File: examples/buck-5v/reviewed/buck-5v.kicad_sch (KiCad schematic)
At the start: 11 parts, among them J1 12V IN, J2 5V OUT, U1 LM2596S-5

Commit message: Route the sheets, and anchor the ground vias where the loop is
The user's verdict on the last round stood: none of the five schematics
read as a human drawing, and the artwork still had its physics wrong.
This round answers both.

The schematic side replaces the stub-and-label sheet with a router.
Every signal net becomes a tree of straight, L-, Z- and detour-shaped
runs on the 1.27 mm grid: legs leave a pin along its own stub, escape
distances stagger so a bus does not fight over one column, every pin
reserves a runway another wire may cross but not ride along, and the
sheet frame, title block and notes are obstacles like any symbol.
Fragments merge Kruskal-style so a rail whose regulator is boxed in
still gets its capacitors chained; each surviving fragment keeps one
label, because the label is what names the net. Collinear same-net
segments are unioned and then split at every tee - KiCad 9's
connectivity requires files drawn the way the editor draws them, with
a junction dot and a wire break wherever a branch tees in, and a wire
that runs through a junction connects on one side of it only. That
last fact cost an evening and is now a comment.

Trying to draw the wires found what no rule had: the buck's LED was
upside down with its ground pointing up into the resistor above it,
both breakout headers faced away from everything they connect to
(fixed with mirrored symbols, which Part now supports), the FPGA
sheet's notes printed over the 1.2 V regulator, and its programming
header sat inside the title block. Wired: buck, motor and op-amp
completely; the Pico carrier 31 of 33 nets; the FPGA board 16 of 19 -
what stays labelled is what a human would label too.

The artwork side anchors every FPGA decoupling capacitor's ground via
against its own pad, on the far side from the supply pad, with the
1.2 mm stub as the whole loop - retiring all seven
layout.decoupling_via findings and that waiver with them. A back_cost
experiment (0.4 to 0.6) to shrink the return-path cuts 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
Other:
- moved on the sheet: D2
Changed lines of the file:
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@@
   	(comment 2 "from tools/make_examples.py in sabas0ba/kicad_skills")
   )
+  (wire (pts (xy 199.39 77.47) (xy 199.39 82.55)) (stroke (width 0) (type default)))
+  (wire (pts (xy 124.46 68.58) (xy 124.46 76.2)) (stroke (width 0) (type default)))
+  (wire (pts (xy 124.46 76.2) (xy 134.62 76.2)) (stroke (width 0) (type default)))
+  (wire (pts (xy 134.62 59.69) (xy 134.62 76.2)) (stroke (width 0) (type default)))
+  (wire (pts (xy 134.62 59.69) (xy 154.94 59.69)) (stroke (width 0) (type default)))
+  (junction (at 134.62 76.2) (diameter 0) (color 0 0 0 0))
   (wire (pts (xy 33.02 66.04) (xy 30.48 66.04)) (stroke (width 0) (type default)))
   (symbol (lib_id "power:+12V") (at 30.48 66.04 90) (unit 1)
@@
   )
   (wire (pts (xy 137.16 76.2) (xy 134.62 76.2)) (stroke (width 0) (type default)))
-  (label "SW" (at 134.62 76.2 0) (effects (font (size 1.27 1.27)) (justify left bottom)))
   (wire (pts (xy 144.78 76.2) (xy 147.32 76.2)) (stroke (width 0) (type default)))
   (symbol (lib_id "power:GND") (at 147.32 76.2 270) (unit 1)
@@
   )
   (wire (pts (xy 154.94 62.23) (xy 154.94 59.69)) (stroke (width 0) (type default)))
-  (label "SW" (at 154.94 59.69 0) (effects (font (size 1.27 1.27)) (justify left bottom)))
   (wire (pts (xy 154.94 69.85) (xy 154.94 72.39)) (stroke (width 0) (type default)))
   (symbol (lib_id "power:+5V") (at 154.94 72.39 0) (unit 1)
@@
     (instances (project "buck-5v" (path "/ec98644d-848c-5056-a4cb-c829189be5c3" (reference "R1") (unit 1))))
   )
-  (wire (pts (xy 199.39 85.09) (xy 199.39 82.55)) (stroke (width 0) (type default)))
-  (symbol (lib_id "power:GND") (at 199.39 82.55 180) (unit 1)
-    (exclude_from_sim no) (in_bom no) (on_board yes) (dnp no)
-    (property "Reference" "#PWR18" (at 199.39 82.55 0) (effects (font (size 1.27 1.27)) hide))
-    (property "Value" "GND" (at 199.39 78.74 0) (effects (font (size 1.27 1.27))))
-    (property "Footprint" "" (at 199.39 82.55 0) (effects (font (size 1.27 1.27)) hide))
-    (property "Datasheet" "" (at 199.39 82.55 0) (effects (font (size 1.27 1.27)) hide))
+  (wire (pts (xy 199.39 92.71) (xy 199.39 95.25)) (stroke (width 0) (type default)))
+  (symbol (lib_id "power:GND") (at 199.39 95.25 0) (unit 1)
+    (exclude_from_sim no) (in_bom no) (on_board yes) (dnp no)
+    (property "Reference" "#PWR18" (at 199.39 95.25 0) (effects (font (size 1.27 1.27)) hide))
+    (property "Value" "GND" (at 199.39 99.06 0) (effects (font (size 1.27 1.27))))
+    (property "Footprint" "" (at 199.39 95.25 0) (effects (font (size 1.27 1.27)) hide))
+    (property "Datasheet" "" (at 199.39 95.25 0) (effects (font (size 1.27 1.27)) hide))
     (pin "1" (uuid "3235223e-d87f-580f-9e80-34d8bd5b48e9-p"))
     (instances (project "buck-5v" (path "/ec98644d-848c-5056-a4cb-c829189be5c3" (reference "#PWR18") (unit 1))))
   )
-  (wire (pts (xy 199.39 92.71) (xy 199.39 95.25)) (stroke (width 0) (type default)))
-  (label "LED_A" (at 199.39 95.25 0) (effects (font (size 1.27 1.27)) (justify left bottom)))
-  (symbol (lib_id "Device:LED") (at 199.39 88.9 270.0) (unit 1)
+  (wire (pts (xy 199.39 85.09) (xy 199.39 82.55)) (stroke (width 0) (type default)))
+  (symbol (lib_id "Device:LED") (at 199.39 88.9 90.0) (unit 1)
     (exclude_from_sim no) (in_bom yes) (on_board yes) (dnp no)
     (property "Reference" "D2" (at 199.39 82.55 0) (effects (font (size 1.27 1.27))))
@@
     (instances (project "buck-5v" (path "/ec98644d-848c-5056-a4cb-c829189be5c3" (reference "J2") (unit 1))))
   )
-  (wire (pts (xy 53.34 118.11) (xy 53.34 120.65)) (stroke (width 0) (type default)) (uuid "50121226-b759-5cf7-9474-3f9038b2192a-w"))
-  (label "+12V" (at 53.34 120.65 0) (effects (font (size 1.27 1.27)) (justify left bottom)) (uuid "50121226-b759-5cf7-9474-3f9038b2192a-l"))
-  (symbol (lib_id "power:PWR_FLAG") (at 53.34 118.11 0) (unit 1)
-    (exclude_from_sim no) (in_bom no) (on_board yes) (dnp no)
-    (property "Reference" "#FLG01" (at 53.34 118.11 0) (effects (font (size 1.27 1.27)) hide))
-    (property "Value" "PWR_FLAG" (at 53.34 114.3 0) (effects (font (size 1.27 1.27))))
-    (property "Footprint" "" (at 53.34 118.11 0) (effects (font (size 1.27 1.27)) hide))
-    (property "Datasheet" "" (at 53.34 118.11 0) (effects (font (size 1.27 1.27)) hide))
+  (wire (pts (xy 74.92999999999999 35.56) (xy 74.92999999999999 38.1)) (stroke (width 0) (type default)) (uuid "50121226-b759-5cf7-9474-3f9038b2192a-w"))
+  (label "+12V" (at 74.92999999999999 38.1 0) (effects (font (size 1.27 1.27)) (justify left bottom)) (uuid "50121226-b759-5cf7-9474-3f9038b2192a-l"))
+  (symbol (lib_id "power:PWR_FLAG") (at 74.92999999999999 35.56 0) (unit 1)
+    (exclude_from_sim no) (in_bom no) (on_board yes) (dnp no)
+    (property "Reference" "#FLG01" (at 74.92999999999999 35.56 0) (effects (font (size 1.27 1.27)) hide))
+    (property "Value" "PWR_FLAG" (at 74.92999999999999 31.750000000000004 0) (effects (font (size 1.27 1.27))))
+    (property "Footprint" "" (at 74.92999999999999 35.56 0) (effects (font (size 1.27 1.27)) hide))
+    (property "Datasheet" "" (at 74.92999999999999 35.56 0) (effects (font (size 1.27 1.27)) hide))
     (pin "1" (uuid "50121226-b759-5cf7-9474-3f9038b2192a-p"))
     (instances (project "buck-5v" (path "/ec98644d-848c-5056-a4cb-c829189be5c3" (reference "#FLG01") (unit 1))))
   )
-  (wire (pts (xy 68.58 118.11) (xy 68.58 120.65)) (stroke (width 0) (type default)) (uuid "826d4f09-5262-50fb-a7d7-fd8ef58ef78c-w"))
-  (label "GND" (at 68.58 120.65 0) (effects (font (size 1.27 1.27)) (justify left bottom)) (uuid "826d4f09-5262-50fb-a7d7-fd8ef58ef78c-l"))
-  (symbol (lib_id "power:PWR_FLAG") (at 68.58 118.11 0) (unit 1)
-    (exclude_from_sim no) (in_bom no) (on_board yes) (dnp no)
-    (property "Reference" "#FLG02" (at 68.58 118.11 0) (effects (font (size 1.27 1.27)) hide))
-    (property "Value" "PWR_FLAG" (at 68.58 114.3 0) (effects (font (size 1.27 1.27))))
-    (property "Footprint" "" (at 68.58 118.11 0) (effects (font (size 1.27 1.27)) hide))
-    (property "Datasheet" "" (at 68.58 118.11 0) (effects (font (size 1.27 1.27)) hide))
+  (wire (pts (xy 90.17 35.56) (xy 90.17 38.1)) (stroke (width 0) (type default)) (uuid "826d4f09-5262-50fb-a7d7-fd8ef58ef78c-w"))
+  (label "GND" (at 90.17 38.1 0) (effects (font (size 1.27 1.27)) (justify left bottom)) (uuid "826d4f09-5262-50fb-a7d7-fd8ef58ef78c-l"))
+  (symbol (lib_id "power:PWR_FLAG") (at 90.17 35.56 0) (unit 1)
+    (exclude_from_sim no) (in_bom no) (on_board yes) (dnp no)
+    (property "Reference" "#FLG02" (at 90.17 35.56 0) (effects (font (size 1.27 1.27)) hide))
+    (property "Value" "PWR_FLAG" (at 90.17 31.750000000000004 0) (effects (font (size 1.27 1.27))))
+    (property "Footprint" "" (at 90.17 35.56 0) (effects (font (size 1.27 1.27)) hide))
+    (property "Datasheet" "" (at 90.17 35.56 0) (effects (font (size 1.27 1.27)) hide))
     (pin "1" (uuid "826d4f09-5262-50fb-a7d7-fd8ef58ef78c-p"))
     (instances (project "buck-5v" (path "/ec98644d-848c-5056-a4cb-c829189be5c3" (reference "#FLG02") (unit 1))))
   )
-  (wire (pts (xy 83.82 118.11) (xy 83.82 120.65)) (stroke (width 0) (type default)) (uuid "838852d4-b251-5697-b727-47601c00fcad-w"))
-  (label "+5V" (at 83.82 120.65 0) (effects (font (size 1.27 1.27)) (justify left bottom)) (uuid "838852d4-b251-5697-b727-47601c00fcad-l"))
-  (symbol (lib_id "power:PWR_FLAG") (at 83.82 118.11 0) (unit 1)
-    (exclude_from_sim no) (in_bom no) (on_board yes) (dnp no)
-    (property "Reference" "#FLG03" (at 83.82 118.11 0) (effects (font (size 1.27 1.27)) hide))
-    (property "Value" "PWR_FLAG" (at 83.82 114.3 0) (effects (font (size 1.27 1.27))))
-    (property "Footprint" "" (at 83.82 118.11 0) (effects (font (size 1.27 1.27)) hide))
-    (property "Datasheet" "" (at 83.82 118.11 0) (effects (font (size 1.27 1.27)) hide))
+  (wire (pts (xy 105.41 35.56) (xy 105.41 38.1)) (stroke (width 0) (type default)) (uuid "838852d4-b251-5697-b727-47601c00fcad-w"))
+  (label "+5V" (at 105.41 38.1 0) (effects (font (size 1.27 1.27)) (justify left bottom)) (uuid "838852d4-b251-5697-b727-47601c00fcad-l"))
+  (symbol (lib_id "power:PWR_FLAG") (at 105.41 35.56 0) (unit 1)
+    (exclude_from_sim no) (in_bom no) (on_board yes) (dnp no)
+    (property "Reference" "#FLG03" (at 105.41 35.56 0) (effects (font (size 1.27 1.27)) hide))
+    (property "Value" "PWR_FLAG" (at 105.41 31.750000000000004 0) (effects (font (size 1.27 1.27))))
+    (property "Footprint" "" (at 105.41 35.56 0) (effects (font (size 1.27 1.27)) hide))
+    (property "Datasheet" "" (at 105.41 35.56 0) (effects (font (size 1.27 1.27)) hide))
     (pin "1" (uuid "838852d4-b251-5697-b727-47601c00fcad-p"))
     (instances (project "buck-5v" (path "/ec98644d-848c-5056-a4cb-c829189be5c3" (reference "#FLG03") (unit 1))))

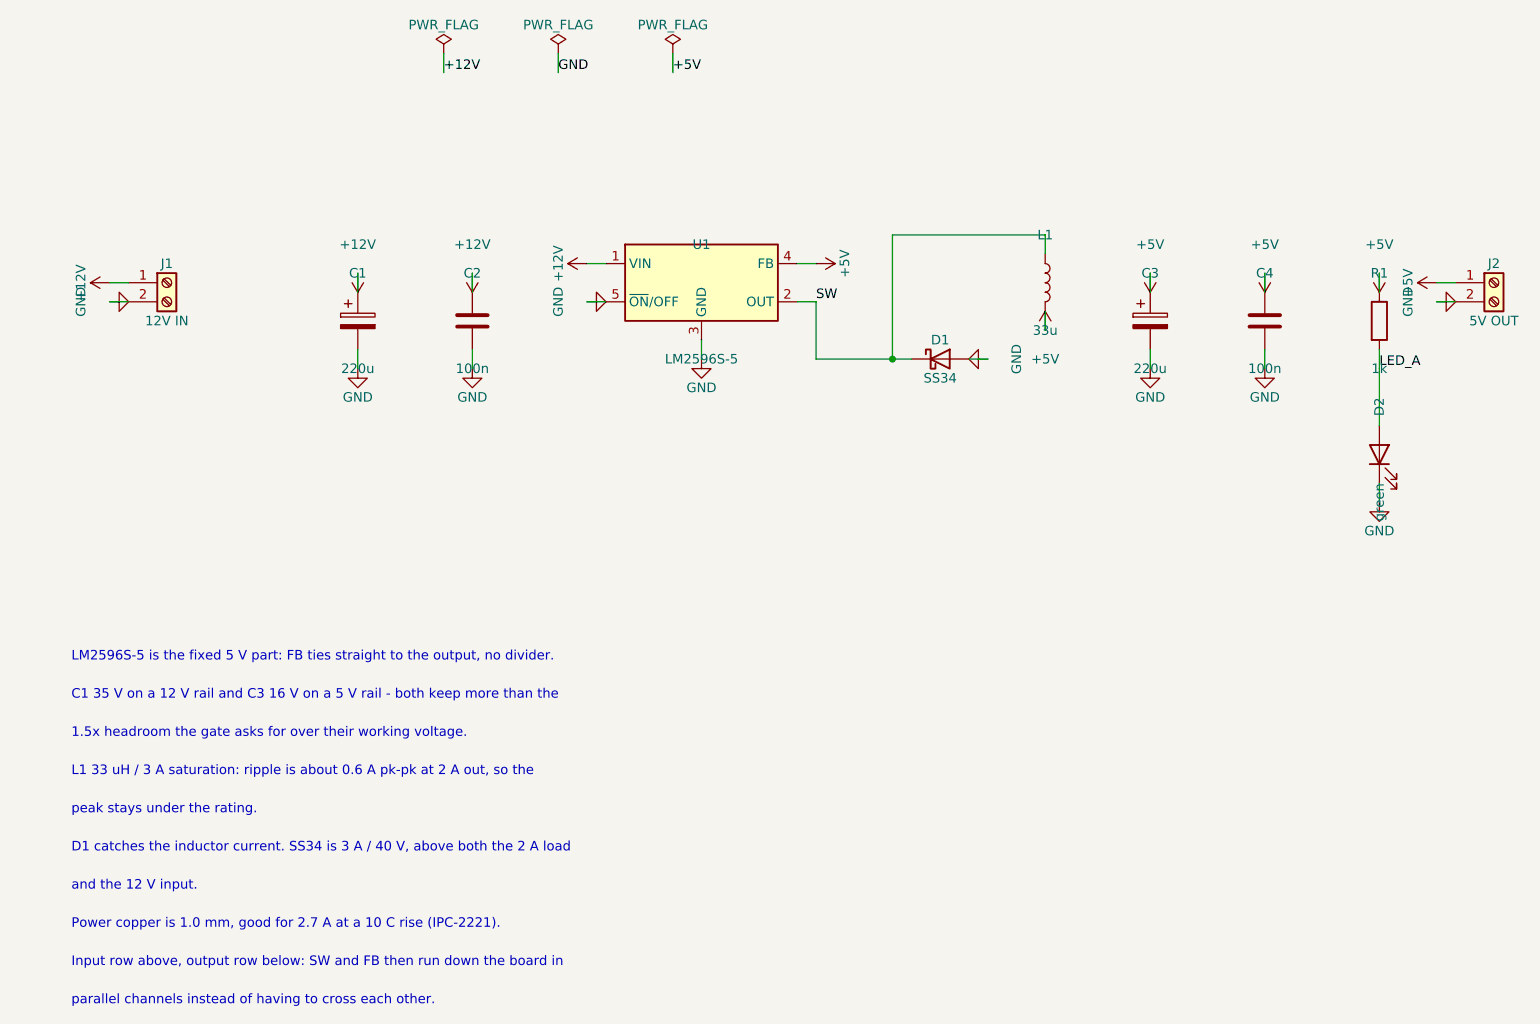
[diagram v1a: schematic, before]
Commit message: Regenerate the five with stitched pours, silk that speaks, and wires that never double back
All ten variants rebuilt by the fixed generator: reviewed boards carry
ground on both faces with the stitching ring (buck 35 vias, fpga 116),
thru_hole_only front pours, the board id and connector pin names in
silk, and the buck's explicit ground return; the sheets hook power up
through upright symbols and source-anchored flags with no overlapping
wires and no junction-less tees left. Every reviewed variant passes its
own gate with zero errors; every as-generated variant still fails, now
also for the rules this round added.

Co-Authored-By: Claude Fable 5 <noreply@anthropic.com>
Claude-Session: https://claude.ai/code/session_01DUj7Ltu92tWg159mCSacwY
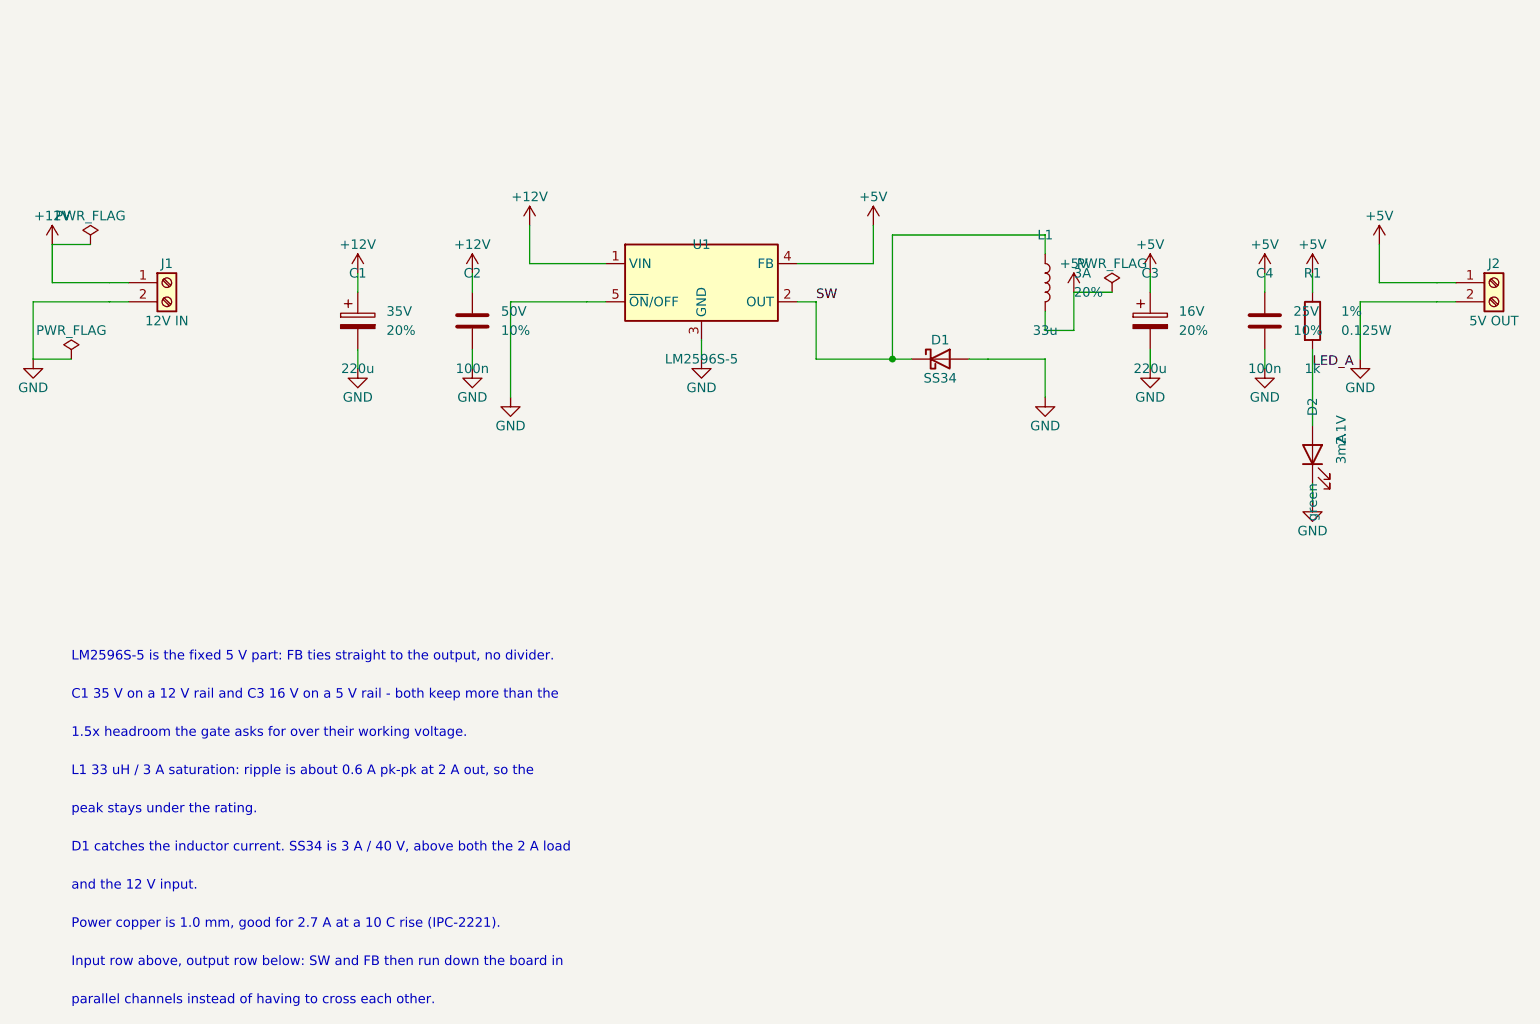
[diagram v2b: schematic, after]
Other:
- moved on the sheet: D2, R1
